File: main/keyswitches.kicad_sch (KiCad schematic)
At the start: 164 parts, among them SW1 SW_Push_45deg, SW10 SW_Push_45deg, SW11 SW_Push_45deg, SW12 SW_Push_45deg, SW13 SW_Push_45deg, SW14 SW_Push_45deg, SW15 SW_Push_45deg, SW16 SW_Push_45deg, SW17 SW_Push_45deg, SW18 SW_Push_45deg, SW19 SW_Push_45deg, SW2 SW_Push_45deg, SW20 SW_Push_45deg, SW21 SW_Push_45deg, SW22 SW_Push_45deg, SW23 SW_Push_45deg, SW24 SW_Push_45deg, SW25 SW_Push_45deg, SW26 SW_Push_45deg, SW27 SW_Push_45deg, SW28 SW_Push_45deg, SW29 SW_Push_45deg, SW3 SW_Push_45deg, SW30 SW_Push_45deg, SW31 SW_Push_45deg, SW32 SW_Push_45deg, SW33 SW_Push_45deg, SW34 SW_Push_45deg, SW35 SW_Push_45deg, SW36 SW_Push_45deg, SW37 SW_Push_45deg, SW38 SW_Push_45deg, SW39 SW_Push_45deg, SW4 SW_Push_45deg, SW40 SW_Push_45deg, SW41 SW_Push_45deg, SW42 SW_Push_45deg, SW43 SW_Push_45deg, SW44 SW_Push_45deg, SW45 SW_Push_45deg, SW46 SW_Push_45deg, SW47 SW_Push_45deg, SW48 SW_Push_45deg, SW49 SW_Push_45deg, SW5 SW_Push_45deg, SW50 SW_Push_45deg, SW51 SW_Push_45deg, SW52 SW_Push_45deg, SW53 SW_Push_45deg, SW54 SW_Push_45deg, SW55 SW_Push_45deg, SW56 SW_Push_45deg, SW57 SW_Push_45deg, SW58 SW_Push_45deg, SW59 SW_Push_45deg, SW6 SW_Push_45deg, SW60 SW_Push_45deg, SW61 SW_Push_45deg, SW62 SW_Push_45deg, SW63 SW_Push_45deg, SW64 SW_Push_45deg, SW65 SW_Push_45deg, SW66 SW_Push_45deg, SW67 SW_Push_45deg, SW68 SW_Push_45deg, SW69 SW_Push_45deg, SW7 SW_Push_45deg, SW70 SW_Push_45deg, SW71 SW_Push_45deg, SW72 SW_Push_45deg, SW73 SW_Push_45deg, SW74 SW_Push_45deg, SW75 SW_Push_45deg, SW76 SW_Push_45deg, SW77 SW_Push_45deg, SW78 SW_Push_45deg, SW79 SW_Push_45deg, SW8 SW_Push_45deg, SW80 SW_Push_45deg, SW81 SW_Push_45deg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

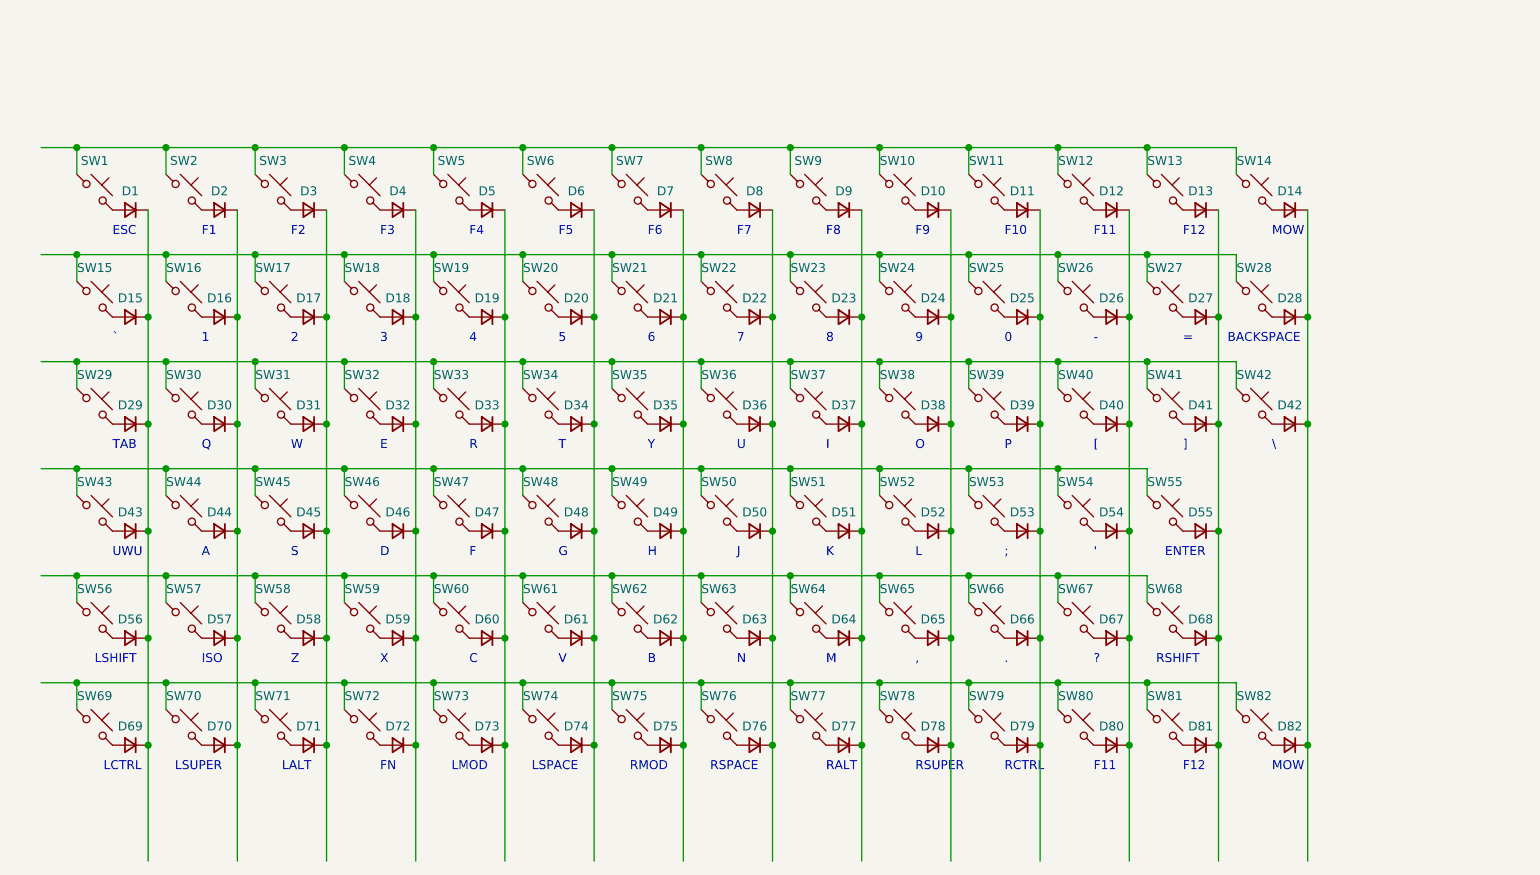
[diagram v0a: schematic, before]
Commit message: Add proposed layout, start LEDs
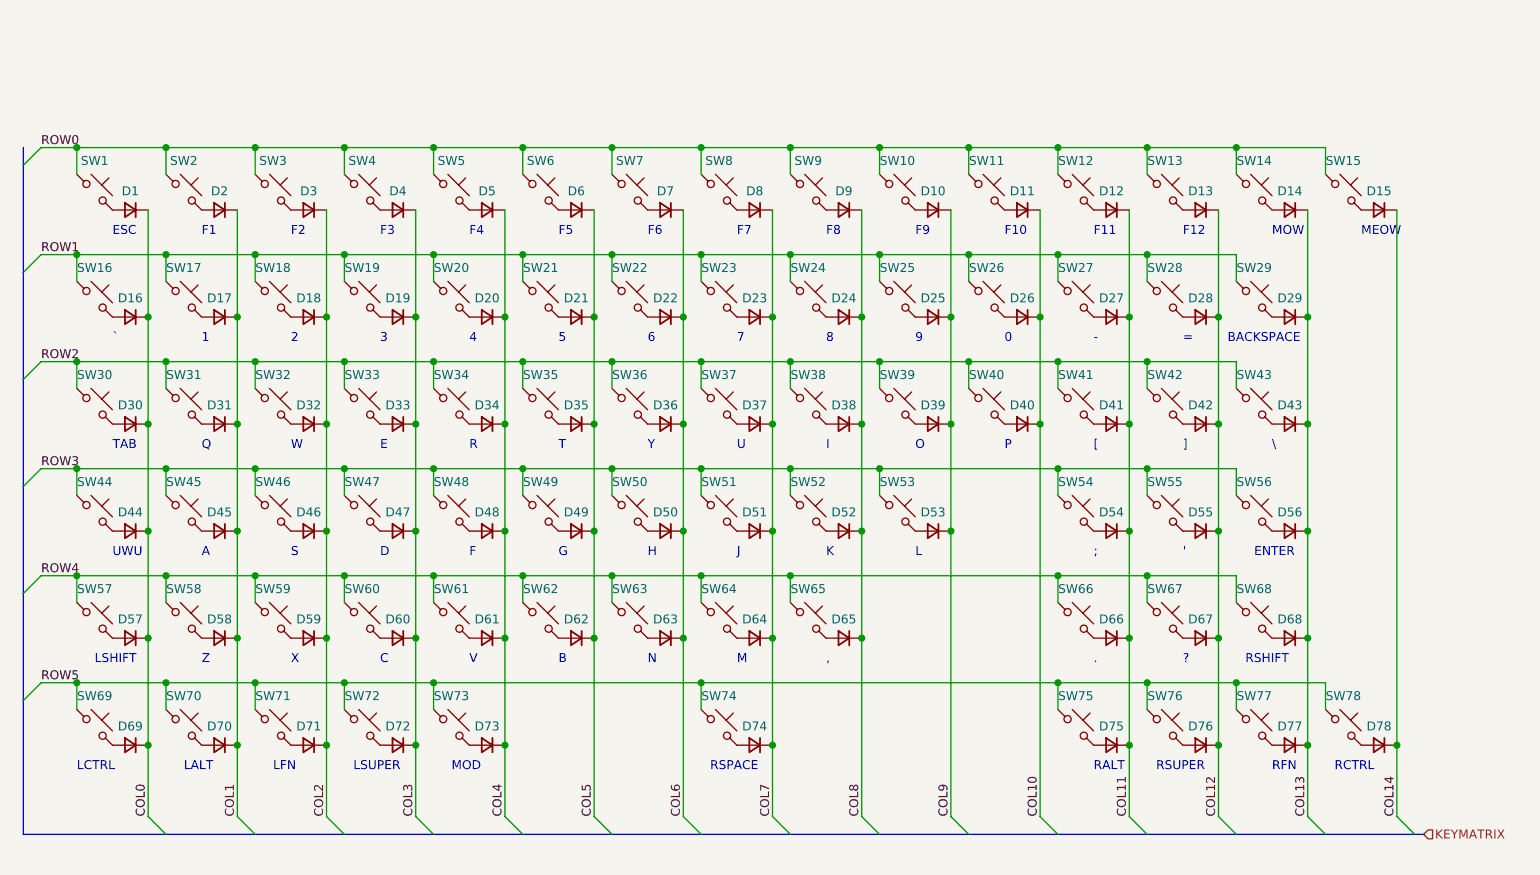
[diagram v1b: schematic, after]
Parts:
- removed D53, D65, D67, D74, D75, D77, D79: D_Small, symbol Device:D_Small
- removed SW53, SW65, SW67, SW74, SW75, SW77, SW79: SW_Push_45deg, keyswitches:SW_PG1350, symbol Switch:SW_Push_45deg
- added D15, D56, D68: D_Small, symbol Device:D_Small
- added SW15, SW56, SW68: SW_Push_45deg, keyswitches:SW_PG1350, symbol Switch:SW_Push_45deg
- renumbered D15 to D16, D16 to D17, D17 to D18, D18 to D19, D19 to D20, D20 to D21, D21 to D22, D22 to D23, D23 to D24, D24 to D25, D25 to D26, D26 to D27, D27 to D28, D28 to D29, D29 to D30, D30 to D31, D31 to D32, D32 to D33, D33 to D34, D34 to D35, D35 to D36, D36 to D37, D37 to D38, D38 to D39, D39 to D40, D40 to D41, D41 to D42, D42 to D43, D43 to D44, D44 to D45, D45 to D46, D46 to D47, D47 to D48, D48 to D49, D49 to D50, D50 to D51, D51 to D52, D52 to D53, D56 to D57, D57 to D58, D58 to D59, D59 to D60, D60 to D61, D61 to D62, D62 to D63, D63 to D64, D64 to D65, D68 to D67, D76 to D74, D80 to D75, D81 to D76, D82 to D77, SW15 to SW16, SW16 to SW17, SW17 to SW18, SW18 to SW19, SW19 to SW20, SW20 to SW21, SW21 to SW22, SW22 to SW23, SW23 to SW24, SW24 to SW25, SW25 to SW26, SW26 to SW27, SW27 to SW28, SW28 to SW29, SW29 to SW30, SW30 to SW31, SW31 to SW32, SW32 to SW33, SW33 to SW34, SW34 to SW35, SW35 to SW36, SW36 to SW37, SW37 to SW38, SW38 to SW39, SW39 to SW40, SW40 to SW41, SW41 to SW42, SW42 to SW43, SW43 to SW44, SW44 to SW45, SW45 to SW46, SW46 to SW47, SW47 to SW48, SW48 to SW49, SW49 to SW50, SW50 to SW51, SW51 to SW52, SW52 to SW53, SW56 to SW57, SW57 to SW58, SW58 to SW59, SW59 to SW60, SW60 to SW61, SW61 to SW62, SW62 to SW63, SW63 to SW64, SW64 to SW65, SW68 to SW67, SW76 to SW74, SW80 to SW75, SW81 to SW76, SW82 to SW77
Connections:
- net ROW2: now reaches SW30.1, SW31.1, SW32.1, SW33.1, SW34.1, SW35.1, SW36.1, SW37.1, SW38.1, SW39.1, SW40.1, SW41.1, SW42.1, SW43.1
- net ROW5: now reaches SW69.1, SW70.1, SW71.1, SW72.1, SW73.1, SW74.1, SW75.1, SW76.1, SW77.1, SW78.1
- net COL7: now reaches D23.1 (K), D37.1 (K), D51.1 (K), D64.1 (K), D74.1 (K), D8.1 (K)
- net COL9: now reaches D10.1 (K), D25.1 (K), D39.1 (K), D53.1 (K)
- net COL9: no longer D78.1 (K)
- net COL2: now reaches D18.1 (K), D3.1 (K), D32.1 (K), D46.1 (K), D59.1 (K), D71.1 (K)
- net COL13: now reaches D14.1 (K), D29.1 (K), D43.1 (K), D77.1 (K)
- net COL13: now also D56.1 (K), D68.1 (K)
- net COL0: now reaches D1.1 (K), D16.1 (K), D30.1 (K), D44.1 (K), D57.1 (K), D69.1 (K)
- net COL12: now reaches D13.1 (K), D28.1 (K), D42.1 (K), D55.1 (K), D67.1 (K), D76.1 (K)
- net COL10: now reaches D11.1 (K), D26.1 (K), D40.1 (K)
- net COL10: no longer D66.1 (K)
- net ROW4: now reaches SW57.1, SW58.1, SW59.1, SW60.1, SW61.1, SW62.1, SW63.1, SW64.1, SW65.1, SW66.1, SW67.1
- net ROW4: now also SW68.1
- net ROW0: now reaches SW1.1, SW10.1, SW11.1, SW12.1, SW13.1, SW14.1, SW2.1, SW3.1, SW4.1, SW5.1, SW6.1, SW7.1, SW8.1, SW9.1
- net ROW0: now also SW15.1
- net ROW3: now reaches SW44.1, SW45.1, SW46.1, SW47.1, SW48.1, SW49.1, SW50.1, SW51.1, SW52.1, SW53.1, SW54.1, SW55.1
- net ROW3: now also SW56.1
- net ROW1: now reaches SW16.1, SW17.1, SW18.1, SW19.1, SW20.1, SW21.1, SW22.1, SW23.1, SW24.1, SW25.1, SW26.1, SW27.1, SW28.1, SW29.1
- net COL5: now reaches D21.1 (K), D35.1 (K), D49.1 (K), D6.1 (K), D62.1 (K)
- net COL4: now reaches D20.1 (K), D34.1 (K), D48.1 (K), D5.1 (K), D61.1 (K), D73.1 (K)
- net COL1: now reaches D17.1 (K), D2.1 (K), D31.1 (K), D45.1 (K), D58.1 (K), D70.1 (K)
- net COL11: now reaches D12.1 (K), D27.1 (K), D41.1 (K), D54.1 (K), D75.1 (K)
- net COL11: now also D66.1 (K)
- net COL6: now reaches D22.1 (K), D36.1 (K), D50.1 (K), D63.1 (K), D7.1 (K)
- net COL3: now reaches D19.1 (K), D33.1 (K), D4.1 (K), D47.1 (K), D60.1 (K), D72.1 (K)
- net COL8: now reaches D24.1 (K), D38.1 (K), D52.1 (K), D65.1 (K), D9.1 (K)
- new net: D56.2 (A), SW56.2
- new net: D15.2 (A), SW15.2
- new net: D68.2 (A), SW68.2
- new net COL14: D15.1 (K), D78.1 (K)
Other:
- note added: "LFN"
- note added: "MEOW"
- note added: "MOD"
- note added: "RFN"
- note removed: "FN"
- note removed: "ISO"
- note removed: "LMOD"
- note removed: "LSPACE"
- note removed: "RMOD"

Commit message: Start placing components
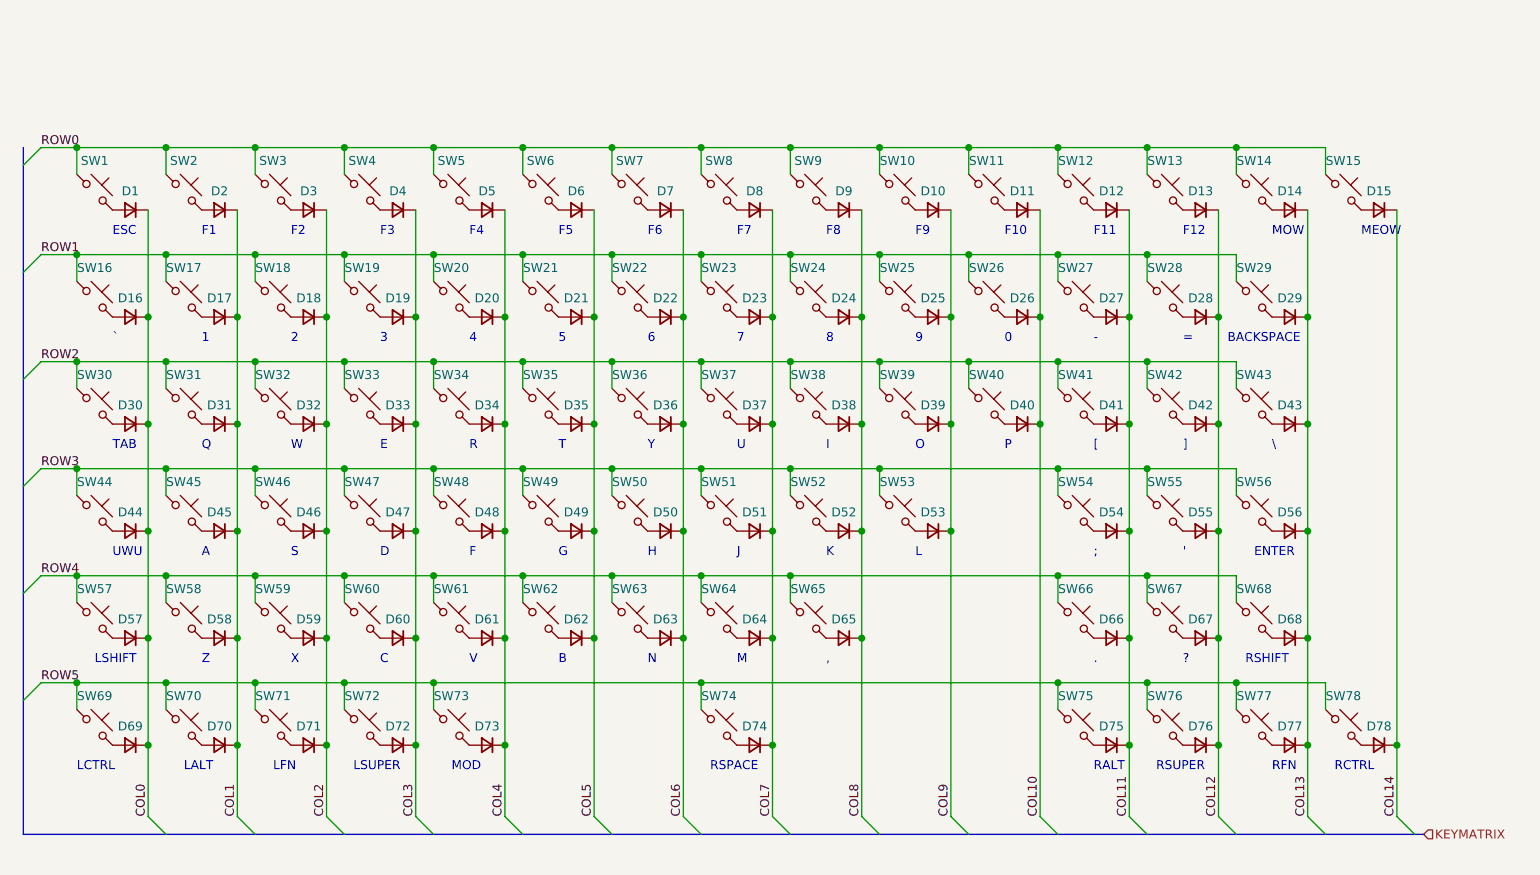
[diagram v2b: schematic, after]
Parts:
- D1, D10, D11, D12, D13, D14, D15, D16, D17, D18, D19, D2, D20, D21, D22, D23, D24, D25, D26, D27, D28, D29, D3, D30, D31, D32, D33, D34, D35, D36, D37, D38, D39, D4, D40, D41, D42, D43, D44, D45, D46, D47, D48, D49, D5, D50, D51, D52, D53, D54, D55, D56, D57, D58, D59, D6, D60, D61, D62, D63, D64, D65, D66, D67, D68, D69, D7, D70, D71, D72, D73, D74, D75, D76, D77, D78, D8, D9: footprint (none) -> Diode_SMD:D_SOD-123F
- SW1, SW10, SW11, SW12, SW13, SW14, SW15, SW16, SW17, SW18, SW19, SW2, SW20, SW21, SW22, SW23, SW24, SW25, SW26, SW27, SW28, SW29, SW3, SW30, SW31, SW32, SW33, SW34, SW35, SW36, SW37, SW38, SW39, SW4, SW40, SW41, SW42, SW43, SW44, SW45, SW46, SW47, SW48, SW49, SW5, SW50, SW51, SW52, SW53, SW54, SW55, SW56, SW57, SW58, SW59, SW6, SW60, SW61, SW62, SW63, SW64, SW65, SW66, SW67, SW68, SW69, SW7, SW70, SW71, SW72, SW73, SW74, SW75, SW76, SW77, SW78, SW8, SW9: footprint keyswitches:SW_PG1350 -> chonc60:Kailh_socket_MX_optional

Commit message: Start placing diodes
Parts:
- SW1, SW10, SW11, SW12, SW13, SW14, SW15, SW16, SW17, SW18, SW19, SW2, SW20, SW21, SW22, SW23, SW24, SW25, SW26, SW27, SW28, SW29, SW3, SW30, SW31, SW32, SW33, SW34, SW35, SW36, SW37, SW38, SW39, SW4, SW40, SW41, SW42, SW43, SW44, SW45, SW46, SW47, SW48, SW49, SW5, SW50, SW51, SW52, SW53, SW54, SW55, SW56, SW57, SW58, SW59, SW6, SW60, SW61, SW62, SW63, SW64, SW65, SW66, SW67, SW68, SW69, SW7, SW70, SW71, SW72, SW73, SW74, SW75, SW76, SW77, SW78, SW8, SW9: footprint chonc60:Kailh_socket_MX_optional -> keyswitches:Kailh_socket_MX

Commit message: Update to new keyboard layout
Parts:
- added D69, D80: D_Small, Diode_SMD:D_SOD-123F, symbol Device:D_Small
- added SW69, SW80: SW_Push_45deg, keyswitches:Kailh_socket_MX, symbol Switch:SW_Push_45deg
- renumbered D69 to D70, D70 to D71, D71 to D72, D72 to D73, D73 to D74, D74 to D75, D75 to D76, D76 to D77, D77 to D78, D78 to D79, SW69 to SW70, SW70 to SW71, SW71 to SW72, SW72 to SW73, SW73 to SW74, SW74 to SW75, SW75 to SW76, SW76 to SW77, SW77 to SW78, SW78 to SW79
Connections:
- net COL10: now also D76.1 (K)
- net COL11: now also D77.1 (K); no longer D76.1 (K)
- net COL12: now also D78.1 (K); no longer D77.1 (K)
- net COL13: now also D79.1 (K); no longer D78.1 (K)
- net COL14: now also D69.1 (K), D80.1 (K); no longer D79.1 (K)
- net ROW4: now also SW69.1
- net ROW5: now also SW80.1; no longer SW76.1
- new net: D69.2 (A), SW69.2
- new net: D80.2 (A), SW80.2
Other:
- note added: "NYAA"
- moved on the sheet: D76, D77, D78, D79, SW76, SW77, SW78, SW79

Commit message: Switch to STM32L063 because I can actually buy those
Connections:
- net ROW5: now also SW76.1
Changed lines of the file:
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@@
   (junction (at 177.8 53.34) (diameter 1.016) (color 0 0 0 0))
   (junction (at 177.8 68.58) (diameter 1.016) (color 0 0 0 0))
+  (junction (at 177.8 114.3) (diameter 1.016) (color 0 0 0 0))
   (junction (at 187.96 62.23) (diameter 1.016) (color 0 0 0 0))
   (junction (at 187.96 77.47) (diameter 1.016) (color 0 0 0 0))
@@
     (stroke (width 0) (type solid) (color 0 0 0 0))
   )
-  (wire (pts (xy 139.7 114.3) (xy 190.5 114.3))
+  (wire (pts (xy 139.7 114.3) (xy 177.8 114.3))
     (stroke (width 0) (type solid) (color 0 0 0 0))
   )
@@
     (stroke (width 0) (type solid) (color 0 0 0 0))
   )
+  (wire (pts (xy 177.8 114.3) (xy 177.8 118.11))
+    (stroke (width 0) (type solid) (color 0 0 0 0))
+  )
+  (wire (pts (xy 177.8 114.3) (xy 190.5 114.3))
+    (stroke (width 0) (type solid) (color 0 0 0 0))
+  )

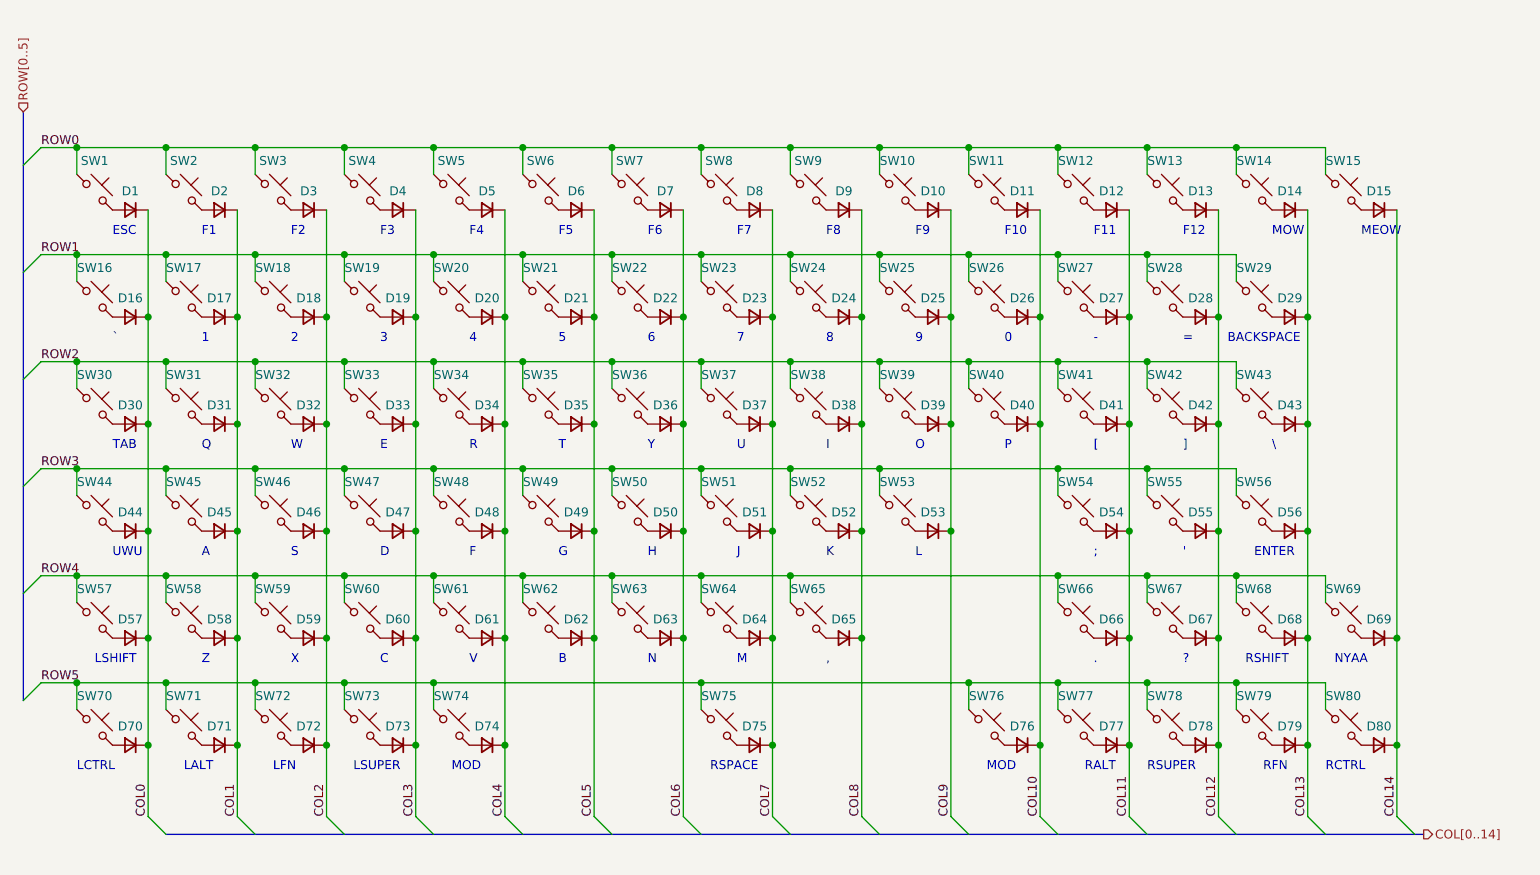
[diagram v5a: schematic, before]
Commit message: Convert to kicad 6.0
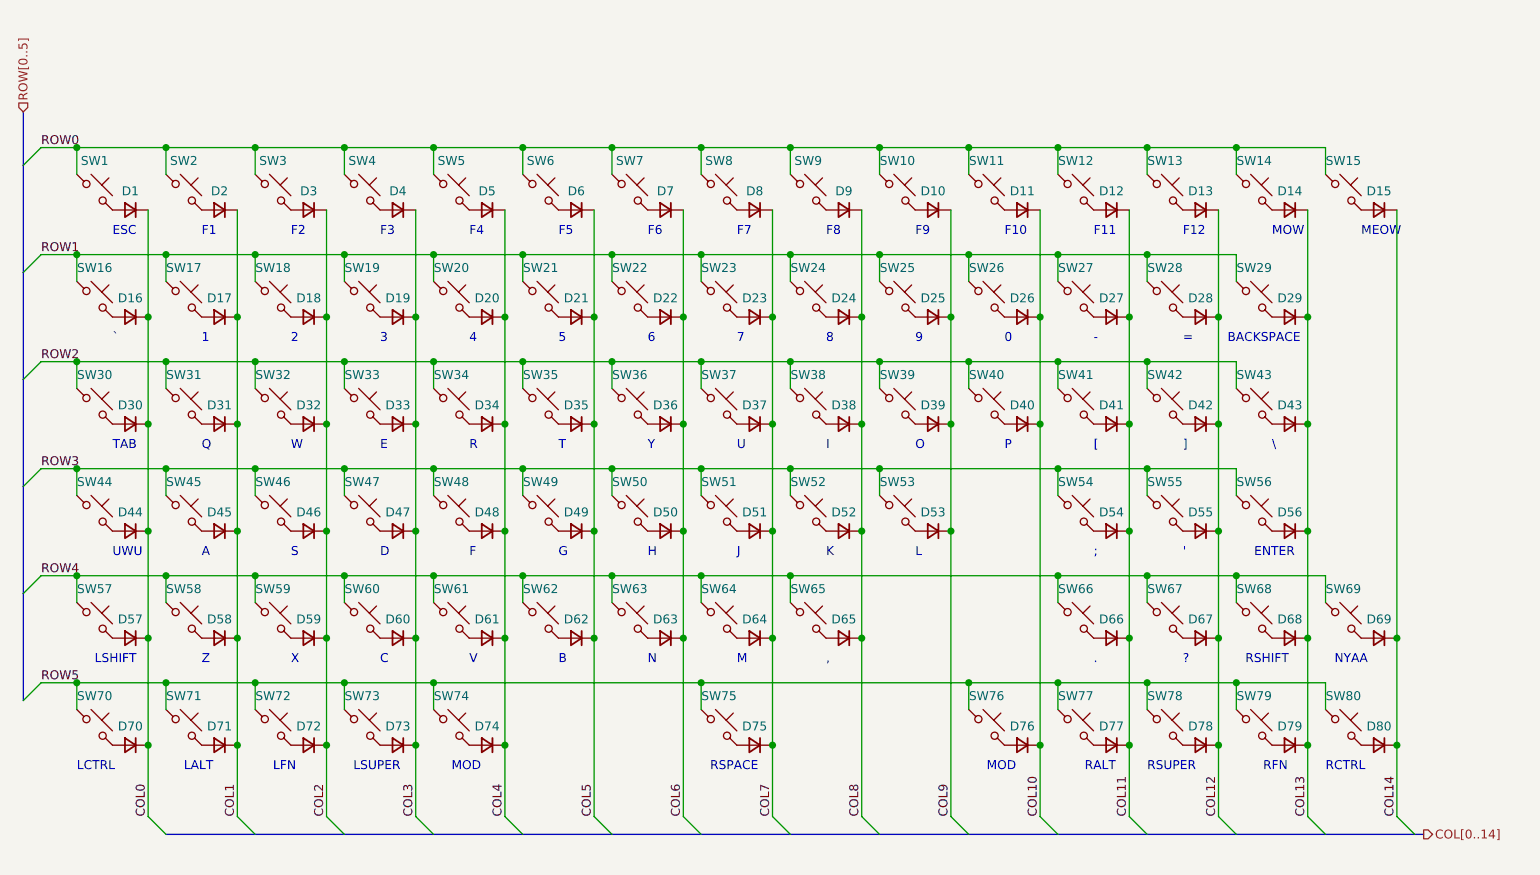
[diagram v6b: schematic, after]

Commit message: Switch to nRF58420 module and battery power
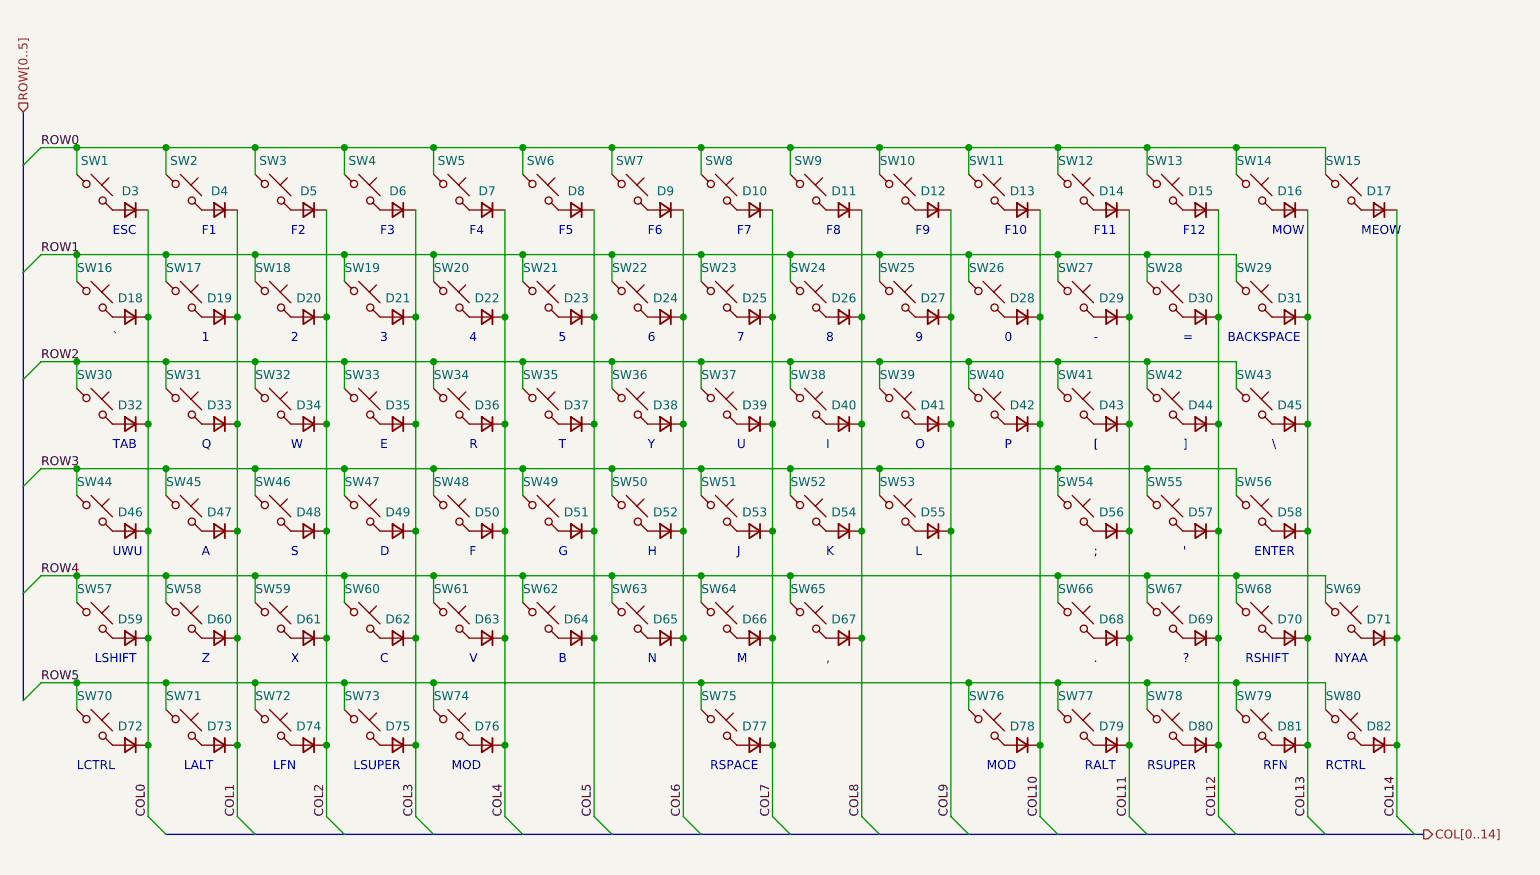
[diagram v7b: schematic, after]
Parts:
- renumbered D8 to D10, D9 to D11, D10 to D12, D11 to D13, D12 to D14, D13 to D15, D14 to D16, D15 to D17, D16 to D18, D17 to D19, D18 to D20, D19 to D21, D20 to D22, D21 to D23, D22 to D24, D23 to D25, D24 to D26, D25 to D27, D26 to D28, D27 to D29, D1 to D3, D28 to D30, D29 to D31, D30 to D32, D31 to D33, D32 to D34, D33 to D35, D34 to D36, D35 to D37, D36 to D38, D37 to D39, D2 to D4, D38 to D40, D39 to D41, D40 to D42, D41 to D43, D42 to D44, D43 to D45, D44 to D46, D45 to D47, D46 to D48, D47 to D49, D3 to D5, D48 to D50, D49 to D51, D50 to D52, D51 to D53, D52 to D54, D53 to D55, D54 to D56, D55 to D57, D56 to D58, D57 to D59, D4 to D6, D58 to D60, D59 to D61, D60 to D62, D61 to D63, D62 to D64, D63 to D65, D64 to D66, D65 to D67, D66 to D68, D67 to D69, D5 to D7, D68 to D70, D69 to D71, D70 to D72, D71 to D73, D72 to D74, D73 to D75, D74 to D76, D75 to D77, D76 to D78, D77 to D79, D6 to D8, D78 to D80, D79 to D81, D80 to D82, D7 to D9

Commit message: Start updating PCB for new design
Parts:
- SW1, SW10, SW11, SW12, SW13, SW14, SW15, SW16, SW17, SW18, SW19, SW2, SW20, SW21, SW22, SW23, SW24, SW25, SW26, SW27, SW28, SW29, SW3, SW30, SW31, SW32, SW33, SW34, SW35, SW36, SW37, SW38, SW39, SW4, SW40, SW41, SW42, SW43, SW44, SW45, SW46, SW47, SW48, SW49, SW5, SW50, SW51, SW52, SW53, SW54, SW55, SW56, SW57, SW58, SW59, SW6, SW60, SW61, SW62, SW63, SW64, SW65, SW66, SW67, SW68, SW69, SW7, SW70, SW71, SW72, SW73, SW74, SW75, SW76, SW77, SW78, SW79, SW8, SW80, SW9: footprint keyswitches:Kailh_socket_MX -> chonc60:SW_PG1350_PG1353
